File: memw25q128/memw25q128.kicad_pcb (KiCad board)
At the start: 2 copper layers, 76.2 x 50.8 mm, 15 parts, among them J1 STM32WORLD_BASE, U1 W25Q128JVS

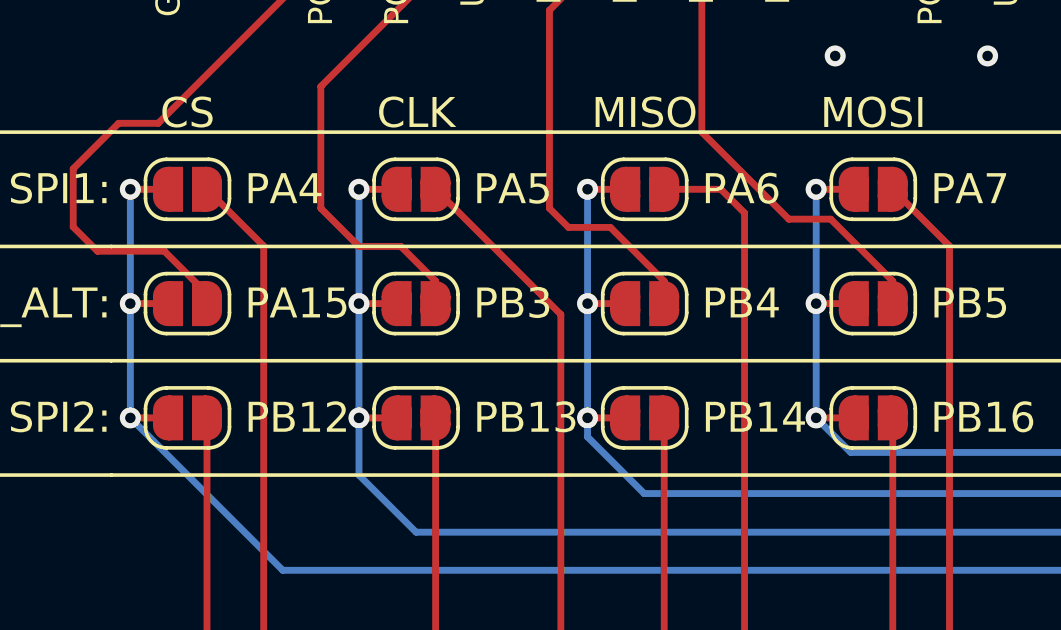
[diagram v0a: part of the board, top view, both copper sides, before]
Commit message: Changed jumpers on memw25qxx
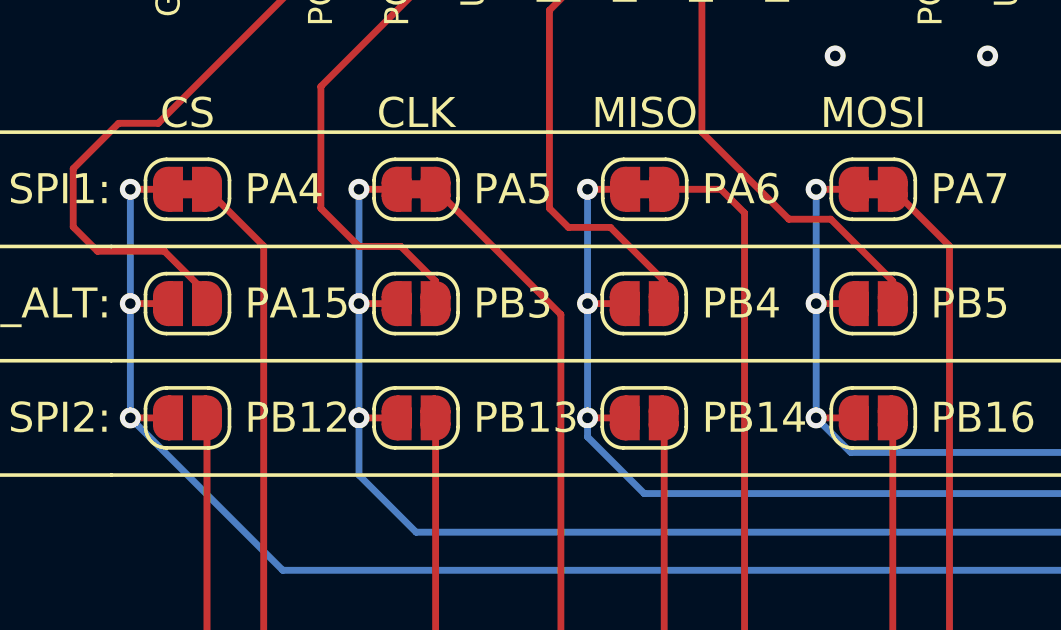
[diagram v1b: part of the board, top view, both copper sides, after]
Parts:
- JP1, JP10, JP4, JP7: value ~ -> SolderJumper_2_Bridged; footprint Jumper:SolderJumper-2_P1.3mm_Open_RoundedPad1.0x1.5mm -> Jumper:SolderJumper-2_P1.3mm_Bridged_RoundedPad1.0x1.5mm
- JP11, JP12, JP2, JP3, JP5, JP6, JP8, JP9: value ~ -> SolderJumper_2_Open
